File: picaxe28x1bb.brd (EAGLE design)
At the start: 38.1 x 59.7 mm, 40 parts, among them Q1 16MHz, U1 PICAXE-28X2, U2 74AHC1G04, U3 74AHC1G04, X1 VIN, X2 GND

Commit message: updated layout, leds, inverted serial, etc.
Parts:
- removed R11, R12: 330, resistor:R0603
- added R6, R8: 330, resistor:R0603
- LED1, LED2, LED3, PWR: device bt_opto:CHIPLED_0603 -> bt_opto:CHIPLED_0805
- S2: value OFF ON -> (none)
- moved C3 138.1 mm to (11.4, 52.6), flipped to the bottom, turned to 90 degrees
- moved C2 132.7 mm to (22.1, 52.8), flipped to the bottom, turned to 270 degrees
- moved U3 131.8 mm to (14.7, 52.6), flipped to the bottom, turned to 180 degrees
- moved U2 131.0 mm to (18.8, 52.6), flipped to the bottom
- moved LED3 104.1 mm to (33.5, 52.6), turned to 270 degrees
- moved LED1 91.8 mm to (33.5, 50.5), turned to 270 degrees
- moved U$10 53.3 mm to (35.6, 9.91), turned to 90 degrees
- moved R5 43.9 mm to (29.0, 52.8), turned to 0 degrees
- moved R4 42.5 mm to (29.0, 50.5), turned to 0 degrees
- moved S2 12.9 mm to (12.4, 2.54)
- moved D1 11.3 mm to (6.60, 49.8)
- moved S1 10.7 mm to (28.2, 55.9)
- moved PWR 9.20 mm to (22.4, 2.54), turned to 180 degrees
- moved R7 9.18 mm to (18.3, 47.0)
- moved LED2 5.98 mm to (24.4, 2.54), turned to 180 degrees
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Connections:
- net C.1: no longer R4.2
- net C.7: now also R8.1
- net N$1: now also R8.2; no longer R4.1
- net N$2: now also R6.2; no longer R5.1
- net N$5: now also R4.2; no longer R11.1
- net N$7: now also R5.2; no longer R12.1
- net RXD: now also R5.1; no longer R12.2
- net TXD: now also R4.1; no longer R11.2
- net VDD: now also R6.1; no longer R5.2
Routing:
- net RXD: track 0.00 -> 31.7 mm, vias 0 -> 1
- net C.1: track 44.7 -> 15.3 mm, vias 2 -> 0
- net VDD: track 125.8 -> 138.1 mm
- net C.7: track 21.1 -> 31.7 mm, vias 1 -> 2
- net RST: track 6.91 -> 17.1 mm
- net N$3: track 3.63 -> 9.35 mm
- net EN: track 13.8 -> 9.85 mm
- net RXI: track 0.00 -> 3.41 mm
- net TXD: track 27.1 -> 30.3 mm, vias 0 -> 1
- net TXO: track 0.59 -> 3.66 mm
- net N$7: track 0.00 -> 2.78 mm
- net N$5: track 0.00 -> 2.67 mm
- net B.0: track 6.35 -> 8.70 mm
- net GND: track 5.26 -> 7.59 mm, vias 1 -> 3
- net N$2: track 3.10 -> 4.05 mm
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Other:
- board text added: "ON"

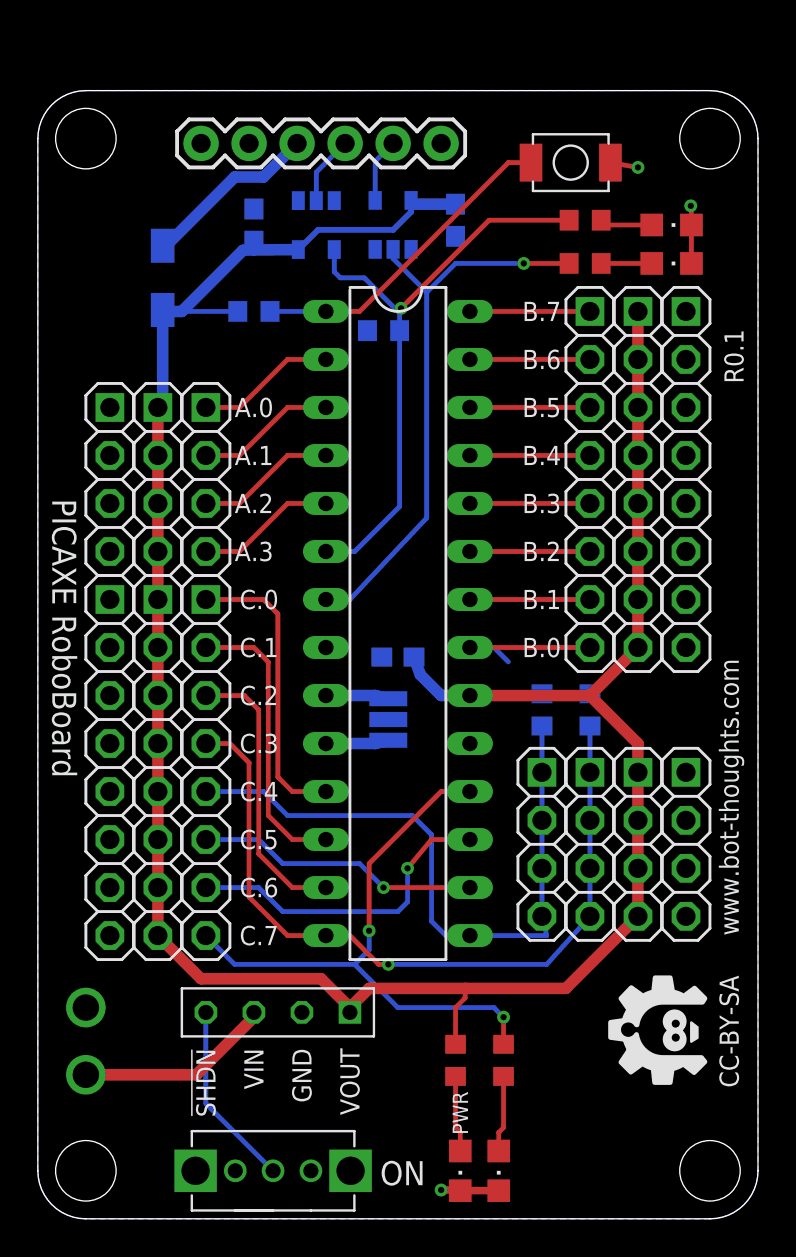
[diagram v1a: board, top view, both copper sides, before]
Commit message: addition of FTDI, usb mini b, layout updates
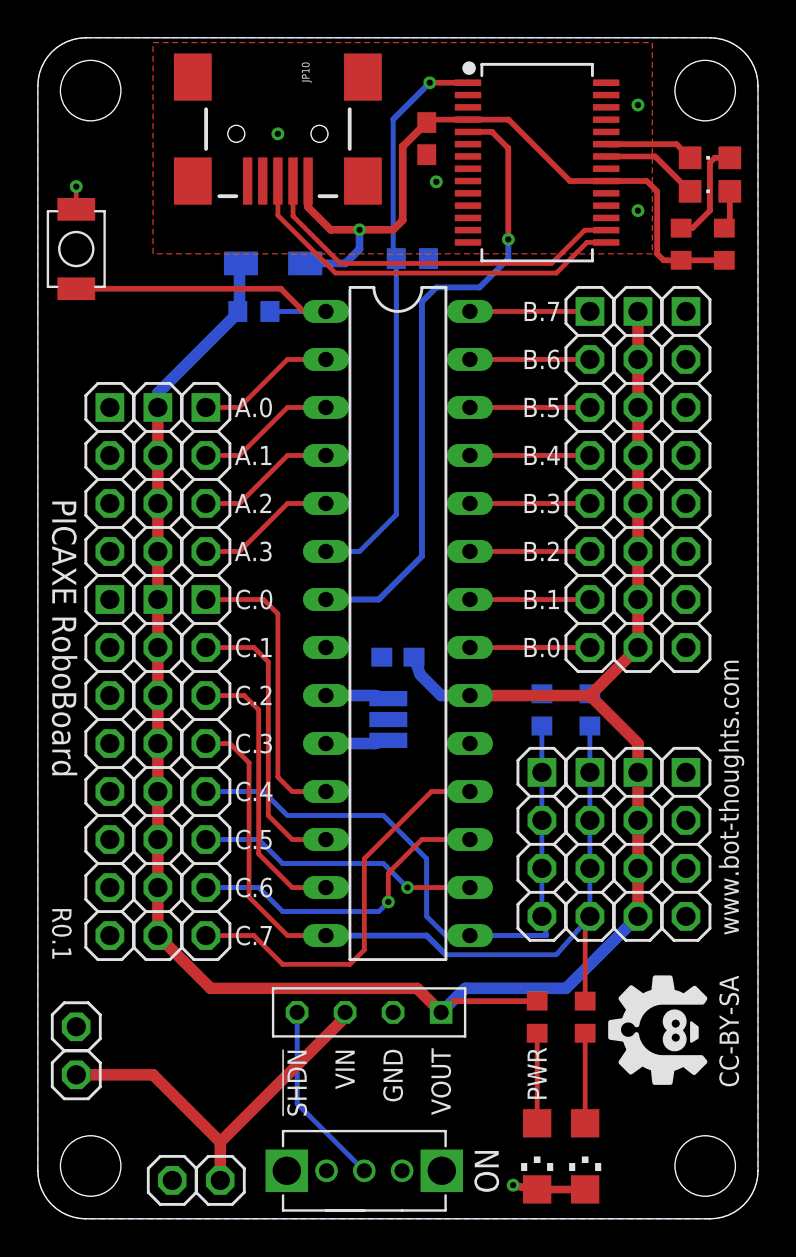
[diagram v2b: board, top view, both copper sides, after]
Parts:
- removed C3: 104, rcl:C0603
- removed U2, U3: 74AHC1G04, 74xx-little-us:SOT23-5
- removed X1: VIN, bt_electromech:PAD_18GA
- removed X2: GND, bt_electromech:PAD_18GA
- added JP10: USB-MINIB, bt_electromech:USB-MINIB
- added JP11: VIN, pinhead-2:1X01-S
- added JP14, JP18: GND, pinhead-2:1X01-S
- added U4: FT232RL, SparkFun-DigitalIC:SSOP28DB
- JP2: value FTDI -> VIN; device SparkFun-Connectors:FTDI_BASIC -> pinhead-2:1X01-S
- LED2: value C.1 -> C.3; device bt_opto:CHIPLED_0805 -> bt_opto:CHIPLED_1206
- PWR: device bt_opto:CHIPLED_0805 -> bt_opto:CHIPLED_1206
- S2: value (none) -> ON/OFF
- moved JP2 52.9 mm to (2.03, 7.62), turned to 90 degrees
- moved S1 26.6 mm to (2.03, 51.3), turned to 270 degrees
- moved R5 7.47 mm to (36.3, 51.6), turned to 90 degrees
- moved LED1 5.95 mm to (35.6, 56.1), turned to 90 degrees
- moved D1 5.89 mm to (12.4, 50.5), turned to 180 degrees
- moved R4 5.18 mm to (34.0, 51.6), turned to 90 degrees
- moved R6 4.89 mm to (26.4, 10.7)
- moved R8 4.89 mm to (29.0, 10.7)
- moved B1 4.83 mm to (17.5, 10.9)
- moved S2 4.83 mm to (17.3, 2.54)
- moved LED2 4.64 mm to (29.0, 3.30)
- moved C2 4.58 mm to (20.6, 57.1), flipped to the top
- moved PWR 4.13 mm to (26.4, 3.30)
- moved R7 4.10 mm to (19.8, 50.8), turned to 180 degrees
- moved LED3 2.70 mm to (35.6, 54.4), turned to 90 degrees
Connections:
- removed net RXI: JP2.RXI, U2.4
- removed net TXO: JP2.TXO, U3.2
- new net N$10: LED3.C, U4.22
- new net N$8: JP10.D-, U4.16
- new net N$9: JP10.D+, U4.15
- new net VBUS: C2.1, D1.A, JP10.VBUS, R4.1, R5.1, U4.20, U4.4
- net C.3: now also R8.1
- net C.7: no longer R8.1
- net GND: now also JP10.GND, JP10.MTN1, JP10.MTN2, JP10.MTN3, JP10.MTN4, JP14.1, JP18.1, U4.18, U4.21, U4.25, U4.26, U4.7; no longer C3.2, JP2.GND, LED1.C, LED3.C, U2.3, U3.3, X2.P$1
- net N$3: now also LED1.C, U4.23; no longer D1.A, JP2.VCC
- net RXD: now also U4.1; no longer R5.1, U3.4
- net TXD: now also U4.5; no longer R4.1, U2.2
- net VDD: no longer C2.1, C3.1, U2.5, U3.5
- net VIN: now also JP11.1, JP2.1; no longer X1.P$1
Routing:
- net VBUS: track 0.00 -> 37.8 mm, vias 0 -> 1
- net N$9: track 0.00 -> 21.1 mm
- net N$8: track 0.00 -> 20.2 mm
- net VDD: track 138.1 -> 123.4 mm
- net C.7: track 31.7 -> 21.2 mm, vias 2 -> 0
- net VIN: track 10.4 -> 20.7 mm
- net N$10: track 0.00 -> 5.20 mm
- net N$3: track 9.35 -> 4.74 mm
- net C.3: track 40.5 -> 44.7 mm, vias 1 -> 0
- net TXO: track 3.66 -> 0.00 mm
- net RXI: track 3.41 -> 0.00 mm
- net TXD: track 30.3 -> 33.3 mm
- net N$5: track 2.67 -> 5.60 mm
- net GND: track 7.59 -> 5.04 mm, vias 3 -> 6
- net B.0: track 8.70 -> 6.35 mm
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- added copper zone on layer 1, net GND
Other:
- board size 38.1 x 59.7 mm -> 38.1 x 62.5 mm
